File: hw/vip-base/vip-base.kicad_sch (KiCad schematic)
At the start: 5 parts, among them J1 USB_C_Receptacle_USB2.0

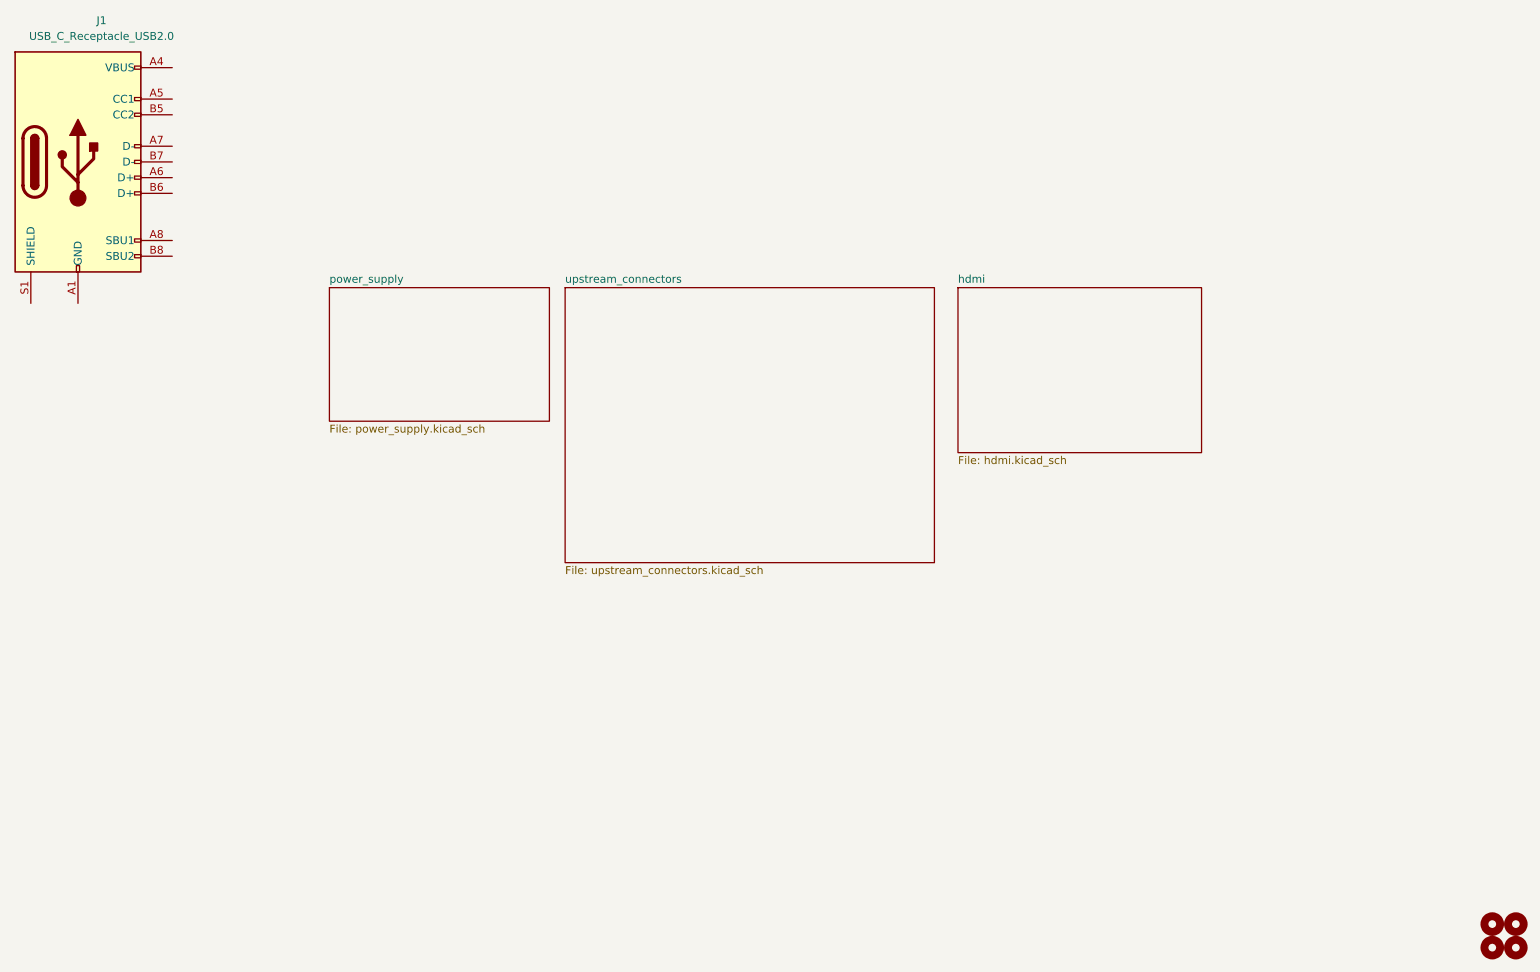
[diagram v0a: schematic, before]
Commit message: hw: Finish main routing
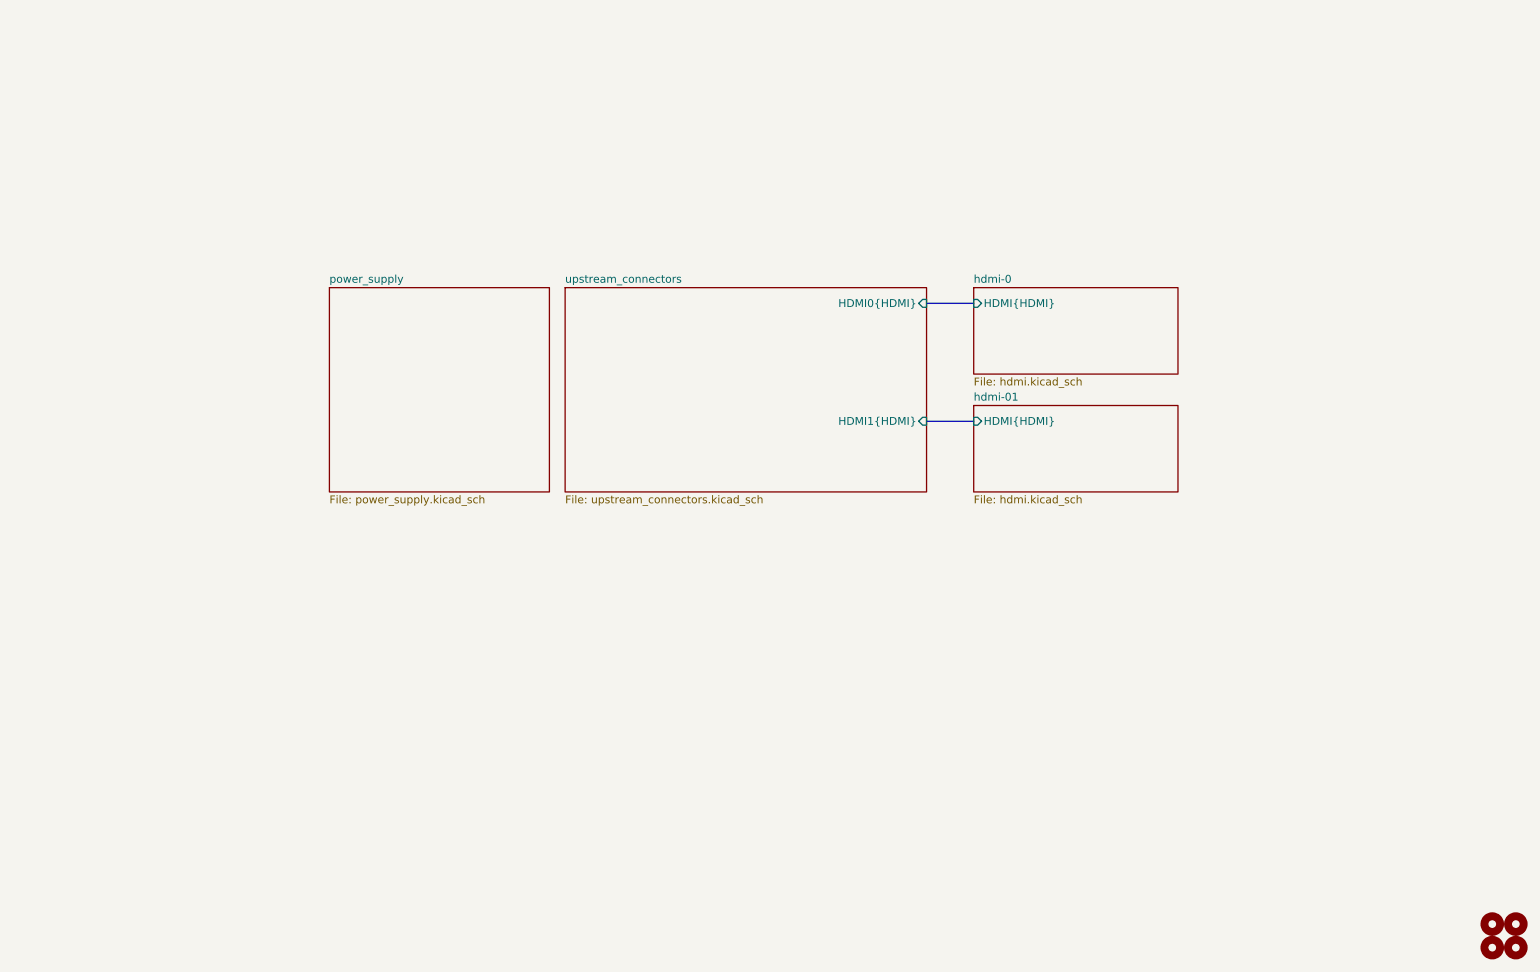
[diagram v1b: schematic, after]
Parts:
- removed J1: USB_C_Receptacle_USB2.0, Connector_USB:USB_C_Receptacle_HRO_TYPE-C-31-M-12, symbol Connector:USB_C_Receptacle_USB2.0
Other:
- sheet hdmi renamed hdmi-0
- added sheet hdmi-01 (hdmi.kicad_sch)
- sheet hdmi-0 ports: added HDMI{HDMI}; removed none
- sheet upstream_connectors ports: added HDMI0{HDMI}, HDMI1{HDMI}; removed none
- company: (none) -> GsD
- title: (none) -> VIP Base
